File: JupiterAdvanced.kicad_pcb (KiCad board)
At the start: 2 copper layers, 314.8 x 162.9 mm, 223 parts, among them SW1 SW_Push, U1 PRTR5V0U2X, U2 AT90USB1286-AU, Y1 16MHz

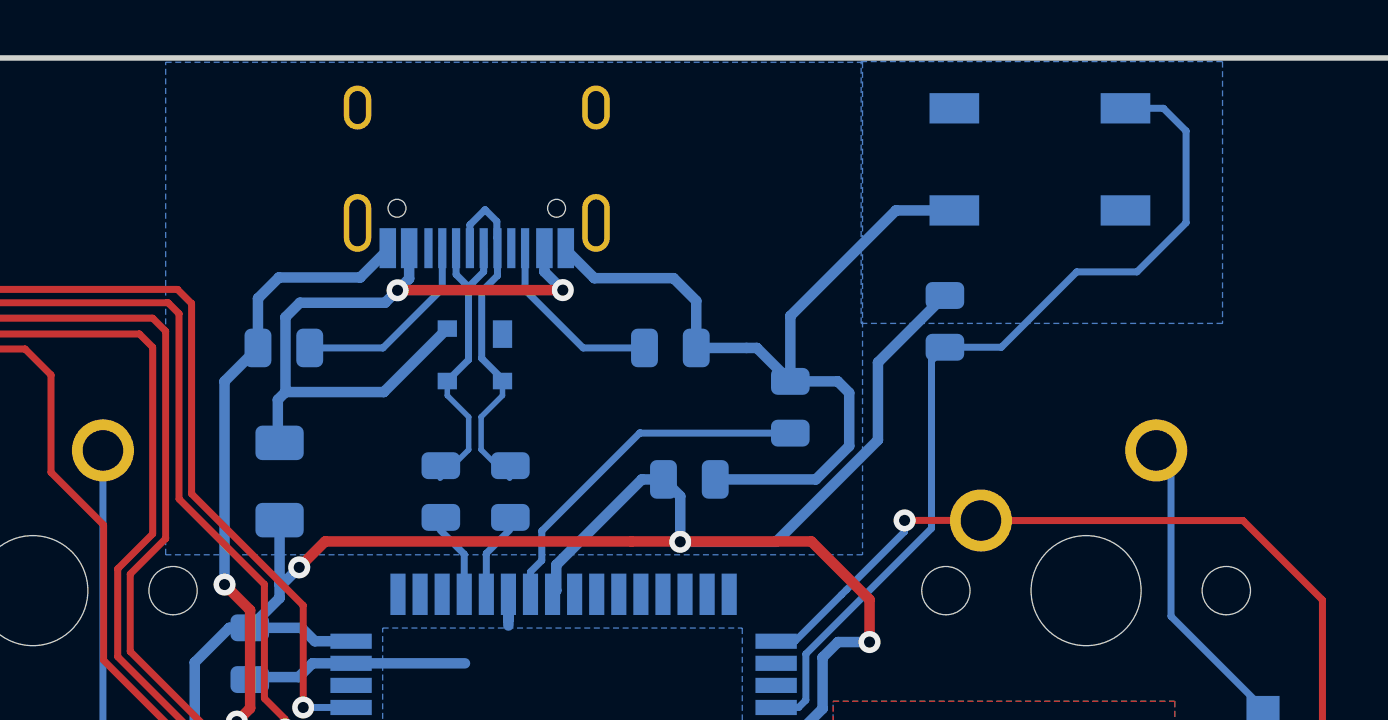
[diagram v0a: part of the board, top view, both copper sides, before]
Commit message: Ferret Bead added on USB Ground
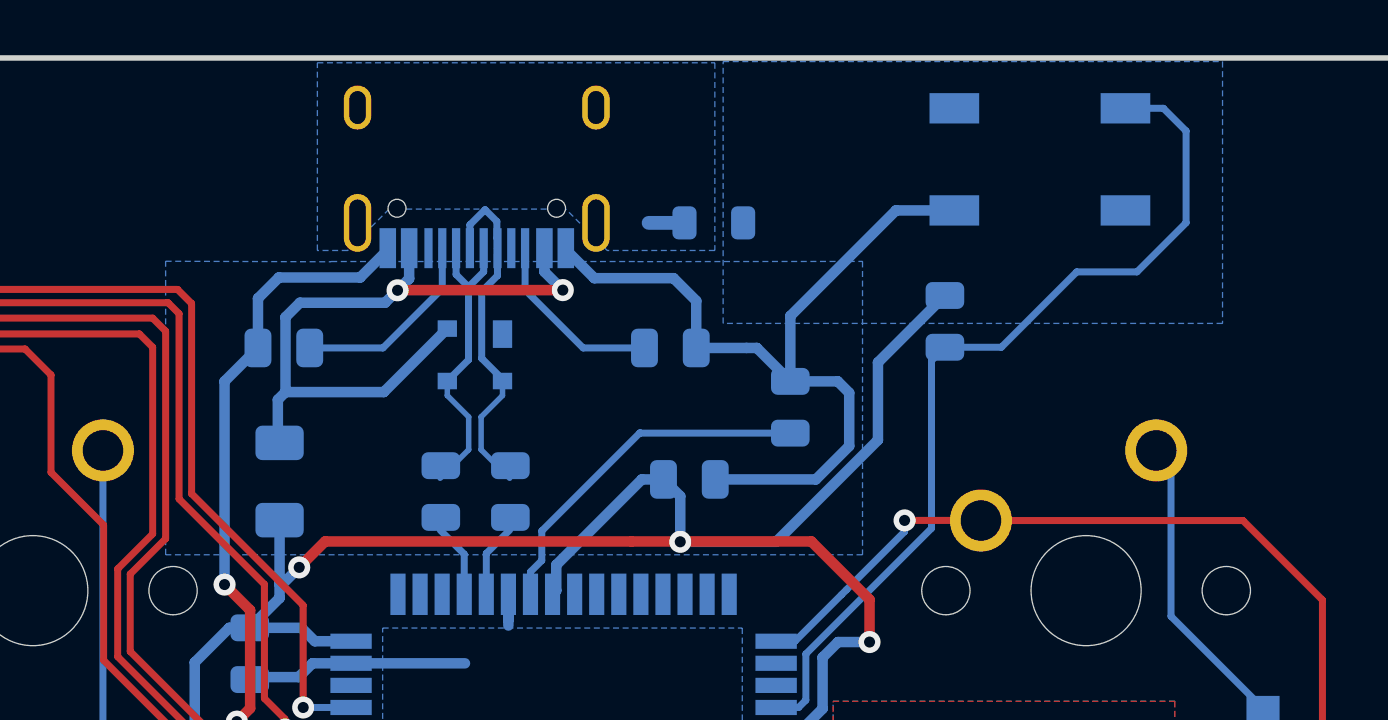
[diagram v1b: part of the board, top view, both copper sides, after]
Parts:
- added FB1: 60@100MHz, Inductor_SMD:L_0805_2012Metric, B.Cu at (271.2, 87.5)
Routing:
- net Earth: track 0.00 -> 1.30 mm

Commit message: Mounting holes updated
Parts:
- H1, H2, H3, H4, H5, H6: footprint MountingHole:MountingHole_2.5mm -> MountingHole:MountingHole_2.5mm_Pad
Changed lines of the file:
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@@
     (add_net VCC)
+  )
+  (module MountingHole:MountingHole_2.5mm_Pad (layer F.Cu)
+    (at 294.02 157.761)
+    (descr "Mounting Hole 2.5mm")
+    (tags "mounting hole 2.5mm")
+    (attr virtual)
+    (fp_text reference H6 (at 0 -3.5) (layer F.SilkS)
+      (effects (font (size 1 1) (thickness 0.15)))
+    )
+    (fp_text value MountingHole (at 0 3.5) (layer F.Fab)
+      (effects (font (size 1 1) (thickness 0.15)))
+    )
+    (fp_text user %R (at 0.3 0) (layer F.Fab)
+      (effects (font (size 1 1) (thickness 0.15)))
+    )
+    (fp_circle (center 0 0) (end 2.5 0) (layer Cmts.User) (width 0.15))
+    (fp_circle (center 0 0) (end 2.75 0) (layer F.CrtYd) (width 0.05))
+    (pad 1 thru_hole circle (at 0 0) (size 5 5) (drill 2.5) (layers *.Cu *.Mask))
+  )
+  (module MountingHole:MountingHole_2.5mm_Pad (layer F.Cu)
+    (at 141.778 157.761)
+    (descr "Mounting Hole 2.5mm")
+    (tags "mounting hole 2.5mm")
+    (attr virtual)
+    (fp_text reference H5 (at 0 -3.5) (layer F.SilkS)
+      (effects (font (size 1 1) (thickness 0.15)))
+    )
+    (fp_text value MountingHole (at 0 3.5) (layer F.Fab)
+      (effects (font (size 1 1) (thickness 0.15)))
+    )
+    (fp_text user %R (at 0.3 0) (layer F.Fab)
+      (effects (font (size 1 1) (thickness 0.15)))
+    )
+    (fp_circle (center 0 0) (end 2.5 0) (layer Cmts.User) (width 0.15))
+    (fp_circle (center 0 0) (end 2.75 0) (layer F.CrtYd) (width 0.05))
+    (pad 1 thru_hole circle (at 0 0) (size 5 5) (drill 2.5) (layers *.Cu *.Mask))
+  )
+  (module MountingHole:MountingHole_2.5mm_Pad (layer F.Cu)
+    (at 65.325 239.475)
+    (descr "Mounting Hole 2.5mm")
+    (tags "mounting hole 2.5mm")
+    (attr virtual)
+    (fp_text reference H4 (at 0 -3.5) (layer F.SilkS)
+      (effects (font (size 1 1) (thickness 0.15)))
+    )
+    (fp_text value MountingHole (at 0 3.5) (layer F.Fab)
+      (effects (font (size 1 1) (thickness 0.15)))
+    )
+    (fp_text user %R (at 0.3 0) (layer F.Fab)
+      (effects (font (size 1 1) (thickness 0.15)))
+    )
+    (fp_circle (center 0 0) (end 2.5 0) (layer Cmts.User) (width 0.15))
+    (fp_circle (center 0 0) (end 2.75 0) (layer F.CrtYd) (width 0.05))
+    (pad 1 thru_hole circle (at 0 0) (size 5 5) (drill 2.5) (layers *.Cu *.Mask))
+  )
+  (module MountingHole:MountingHole_2.5mm_Pad (layer F.Cu)
+    (at 370.325 239.475)
+    (descr "Mounting Hole 2.5mm")
+    (tags "mounting hole 2.5mm")
+    (attr virtual)
+    (fp_text reference H3 (at 0 -3.5) (layer F.SilkS)
+      (effects (font (size 1 1) (thickness 0.15)))
+    )
+    (fp_text value MountingHole (at 0 3.5) (layer F.Fab)
+      (effects (font (size 1 1) (thickness 0.15)))
+    )
+    (fp_text user %R (at 0.3 0) (layer F.Fab)
+      (effects (font (size 1 1) (thickness 0.15)))
+    )
+    (fp_circle (center 0 0) (end 2.5 0) (layer Cmts.User) (width 0.15))
+    (fp_circle (center 0 0) (end 2.75 0) (layer F.CrtYd) (width 0.05))
+    (pad 1 thru_hole circle (at 0 0) (size 5 5) (drill 2.5) (layers *.Cu *.Mask))
+  )
+  (module MountingHole:MountingHole_2.5mm_Pad (layer F.Cu)
+    (at 370.325 86.618)
+    (descr "Mounting Hole 2.5mm")
+    (tags "mounting hole 2.5mm")
+    (attr virtual)
+    (fp_text reference H2 (at 0 -3.5) (layer F.SilkS)
+      (effects (font (size 1 1) (thickness 0.15)))
+    )
+    (fp_text value MountingHole (at 0 3.5) (layer F.Fab)
+      (effects (font (size 1 1) (thickness 0.15)))
+    )
+    (fp_text user %R (at 0.3 0) (layer F.Fab)
+      (effects (font (size 1 1) (thickness 0.15)))
+    )
+    (fp_circle (center 0 0) (end 2.5 0) (layer Cmts.User) (width 0.15))
+    (fp_circle (center 0 0) (end 2.75 0) (layer F.CrtYd) (width 0.05))
+    (pad 1 thru_hole circle (at 0 0) (size 5 5) (drill 2.5) (layers *.Cu *.Mask))
+  )
+  (module MountingHole:MountingHole_2.5mm_Pad (layer F.Cu)
+    (at 65.325 86.518)
+    (descr "Mounting Hole 2.5mm")
+    (tags "mounting hole 2.5mm")
+    (attr virtual)
+    (fp_text reference H1 (at 0 -3.5) (layer F.SilkS)
+      (effects (font (size 1 1) (thickness 0.15)))
+    )
+    (fp_text value MountingHole (at 0 3.5) (layer F.Fab)
+      (effects (font (size 1 1) (thickness 0.15)))
+    )
+    (fp_text user %R (at 0.3 0) (layer F.Fab)
+      (effects (font (size 1 1) (thickness 0.15)))
+    )
+    (fp_circle (center 0 0) (end 2.5 0) (layer Cmts.User) (width 0.15))
+    (fp_circle (center 0 0) (end 2.75 0) (layer F.CrtYd) (width 0.05))
+    (pad 1 thru_hole circle (at 0 0) (size 5 5) (drill 2.5) (layers *.Cu *.Mask))
   )
   (module Inductor_SMD:L_0805_2012Metric (layer B.Cu)
@@
     )
   )
-  (module MountingHole:MountingHole_2.5mm (layer F.Cu)
-    (at 294.02 157.761)
-    (descr "Mounting Hole 2.5mm, no annular")
-    (tags "mounting hole 2.5mm no annular")
-    (attr virtual)
-    (fp_text reference H6 (at 0 -3.5) (layer F.SilkS)
-      (effects (font (size 1 1) (thickness 0.15)))
-    )
-    (fp_text value MountingHole (at 0 3.5) (layer F.Fab)
-      (effects (font (size 1 1) (thickness 0.15)))
-    )
-    (fp_circle (center 0 0) (end 2.5 0) (layer Cmts.User) (width 0.15))
-    (fp_circle (center 0 0) (end 2.75 0) (layer F.CrtYd) (width 0.05))
-    (fp_text user %R (at 0.3 0) (layer F.Fab)
-      (effects (font (size 1 1) (thickness 0.15)))
-    )
-    (pad 1 np_thru_hole circle (at 0 0) (size 2.5 2.5) (drill 2.5) (layers *.Cu *.Mask))
-  )
-  (module MountingHole:MountingHole_2.5mm (layer F.Cu)
-    (at 141.778 157.761)
-    (descr "Mounting Hole 2.5mm, no annular")
-    (tags "mounting hole 2.5mm no annular")
-    (attr virtual)
-    (fp_text reference H5 (at 0 -3.5) (layer F.SilkS)
-      (effects (font (size 1 1) (thickness 0.15)))
-    )
-    (fp_text value MountingHole (at 0 3.5) (layer F.Fab)
-      (effects (font (size 1 1) (thickness 0.15)))
-    )
-    (fp_circle (center 0 0) (end 2.5 0) (layer Cmts.User) (width 0.15))
-    (fp_circle (center 0 0) (end 2.75 0) (layer F.CrtYd) (width 0.05))
-    (fp_text user %R (at 0.3 0) (layer F.Fab)
-      (effects (font (size 1 1) (thickness 0.15)))
-    )
-    (pad 1 np_thru_hole circle (at 0 0) (size 2.5 2.5) (drill 2.5) (layers *.Cu *.Mask))
-  )
-  (module MountingHole:MountingHole_2.5mm (layer F.Cu)
-    (at 65.325 239.475)
-    (descr "Mounting Hole 2.5mm, no annular")
-    (tags "mounting hole 2.5mm no annular")
-    (attr virtual)
-    (fp_text reference H4 (at 0 -3.5) (layer F.SilkS)
-      (effects (font (size 1 1) (thickness 0.15)))
-    )
-    (fp_text value MountingHole (at 0 3.5) (layer F.Fab)
-      (effects (font (size 1 1) (thickness 0.15)))
-    )
-    (fp_circle (center 0 0) (end 2.75 0) (layer F.CrtYd) (width 0.05))
-    (fp_circle (center 0 0) (end 2.5 0) (layer Cmts.User) (width 0.15))
-    (fp_text user %R (at 0.3 0) (layer F.Fab)
-      (effects (font (size 1 1) (thickness 0.15)))
-    )
-    (pad 1 np_thru_hole circle (at 0 0) (size 2.5 2.5) (drill 2.5) (layers *.Cu *.Mask))
-  )
-  (module MountingHole:MountingHole_2.5mm (layer F.Cu)
-    (at 370.325 239.475)
-    (descr "Mounting Hole 2.5mm, no annular")
-    (tags "mounting hole 2.5mm no annular")
-    (attr virtual)
-    (fp_text reference H3 (at 0 -3.5) (layer F.SilkS)
-      (effects (font (size 1 1) (thickness 0.15)))
-    )
-    (fp_text value MountingHole (at 0 3.5) (layer F.Fab)
-      (effects (font (size 1 1) (thickness 0.15)))
-    )
-    (fp_circle (center 0 0) (end 2.75 0) (layer F.CrtYd) (width 0.05))
-    (fp_circle (center 0 0) (end 2.5 0) (layer Cmts.User) (width 0.15))
-    (fp_text user %R (at 0.3 0) (layer F.Fab)
-      (effects (font (size 1 1) (thickness 0.15)))
-    )
-    (pad 1 np_thru_hole circle (at 0 0) (size 2.5 2.5) (drill 2.5) (layers *.Cu *.Mask))
-  )
-  (module MountingHole:MountingHole_2.5mm (layer F.Cu)
-    (at 370.325 86.618)
-    (descr "Mounting Hole 2.5mm, no annular")
-    (tags "mounting hole 2.5mm no annular")
-    (attr virtual)
-    (fp_text reference H2 (at 0 -3.5) (layer F.SilkS)
-      (effects (font (size 1 1) (thickness 0.15)))
-    )
-    (fp_text value MountingHole (at 0 3.5) (layer F.Fab)
-      (effects (font (size 1 1) (thickness 0.15)))
-    )
-    (fp_circle (center 0 0) (end 2.75 0) (layer F.CrtYd) (width 0.05))
-    (fp_circle (center 0 0) (end 2.5 0) (layer Cmts.User) (width 0.15))
-    (fp_text user %R (at 0.3 0) (layer F.Fab)
-      (effects (font (size 1 1) (thickness 0.15)))
-    )
-    (pad 1 np_thru_hole circle (at 0 0) (size 2.5 2.5) (drill 2.5) (layers *.Cu *.Mask))
-  )
-  (module MountingHole:MountingHole_2.5mm (layer F.Cu)
-    (at 65.325 86.518)
-    (descr "Mounting Hole 2.5mm, no annular")
-    (tags "mounting hole 2.5mm no annular")
-    (attr virtual)
-    (fp_text reference H1 (at 0 -3.5) (layer F.SilkS)
-      (effects (font (size 1 1) (thickness 0.15)))
-    )
-    (fp_text value MountingHole (at 0 3.5) (layer F.Fab)
-      (effects (font (size 1 1) (thickness 0.15)))
-    )
-    (fp_circle (center 0 0) (end 2.75 0) (layer F.CrtYd) (width 0.05))
-    (fp_circle (center 0 0) (end 2.5 0) (layer Cmts.User) (width 0.15))
-    (fp_text user %R (at 0.3 0) (layer F.Fab)
-      (effects (font (size 1 1) (thickness 0.15)))
-    )
-    (pad 1 np_thru_hole circle (at 0 0) (size 2.5 2.5) (drill 2.5) (layers *.Cu *.Mask))
-  )
   (module Resistor_SMD:R_0805_2012Metric (layer B.Cu)

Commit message: ATMega32u4 MCU added
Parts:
- removed U2: AT90USB1286-AU, Package_QFP:TQFP-64_14x14mm_P0.8mm
- added U10: ATmega32U4-AU, Package_QFP:TQFP-44_10x10mm_P0.8mm, B.Cu at (265.7, 108.5)
- H1, H2, H3, H4, H5, H6: footprint MountingHole:MountingHole_2.5mm_Pad -> MountingHole:MountingHole_2.5mm
- moved R7 5.09 mm to (260.4, 116.8)
- turned C3 to 90 degrees
- turned C7 to 90 degrees
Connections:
- C7 pad 1: GND -> Net-(C7-Pad1)
- C7 pad 2: Net-(C7-Pad2) -> GND
- R7 pad 1: Net-(R7-Pad1) -> GND
- R7 pad 2: GND -> Net-(R7-Pad2)
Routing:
- net ROW1: track 524.6 -> 497.9 mm
- net ROW2: track 546.7 -> 521.5 mm
- net ROW4: track 584.9 -> 562.3 mm
- net GND: track 119.5 -> 97.0 mm, vias 5 -> 4
- net COL3: track 853.1 -> 831.8 mm
- net ROW5: track 579.1 -> 562.0 mm
- net ROW6: track 620.8 -> 603.7 mm
- net ROW0: track 487.4 -> 470.3 mm
- net Net-(C7-Pad1): track 0.00 -> 15.1 mm
- net COL7: track 188.3 -> 175.3 mm, vias 3 -> 2
- net COL6: track 228.0 -> 215.0 mm, vias 3 -> 2
- net Net-(C7-Pad2): track 12.9 -> 0.00 mm
- net +5V: track 87.0 -> 94.1 mm
- net COL10: track 121.4 -> 128.0 mm
- net COL15: track 243.9 -> 250.2 mm
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
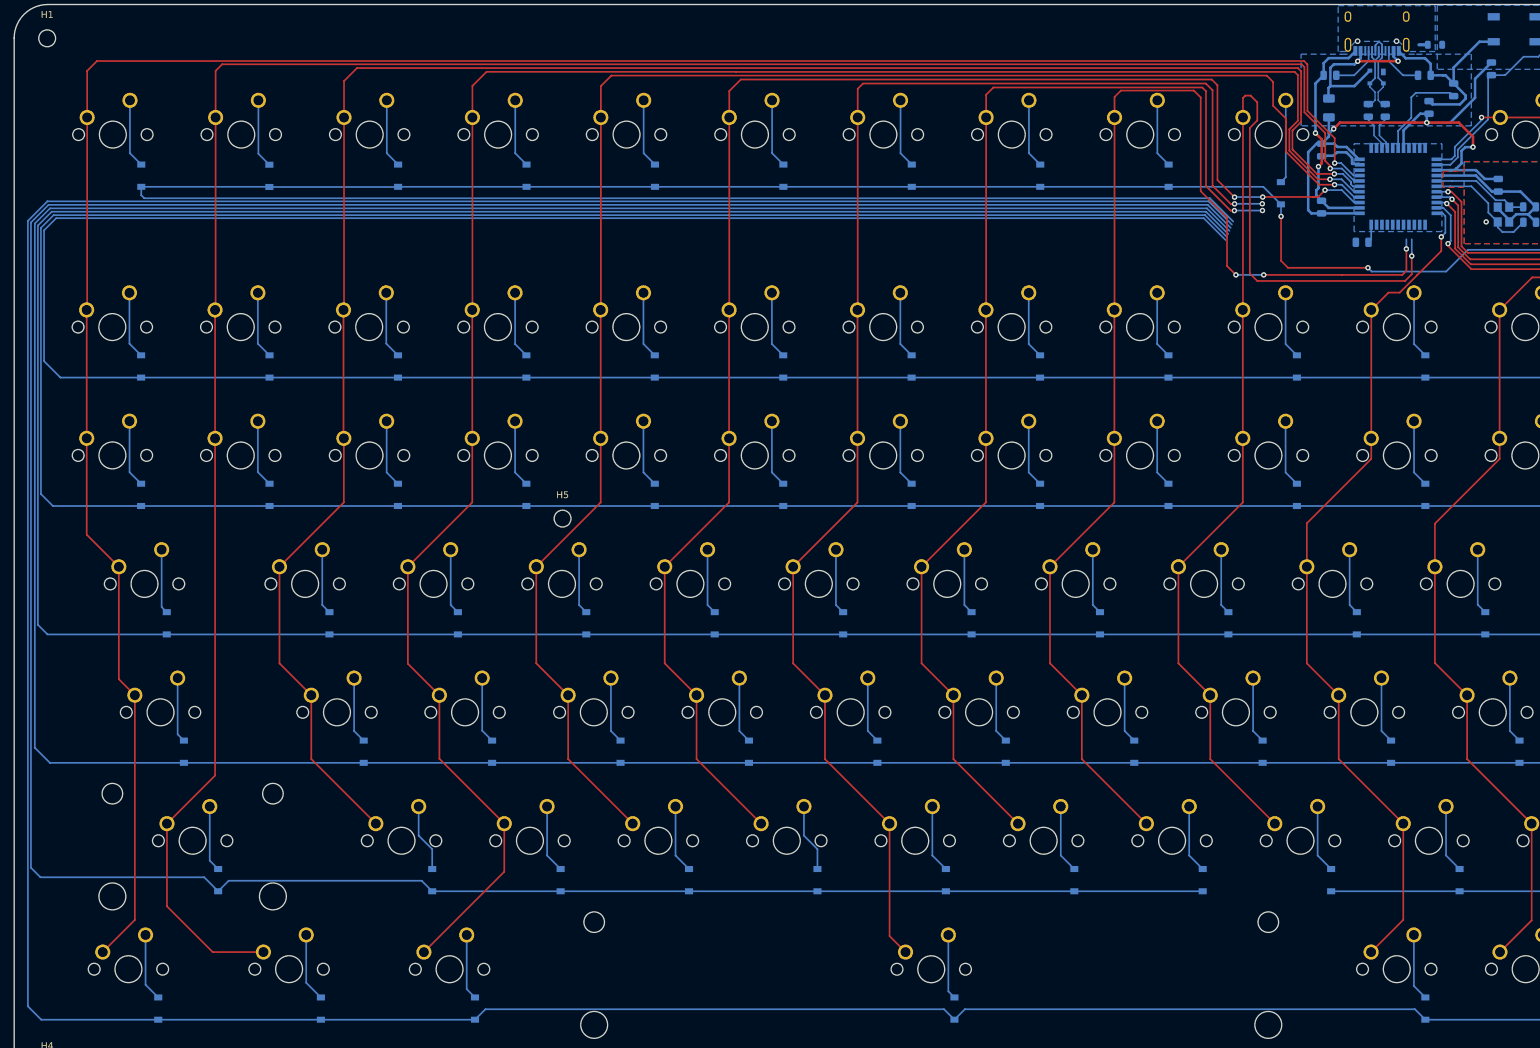
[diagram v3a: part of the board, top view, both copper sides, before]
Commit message: Matrix reconnect, still missing some pins.
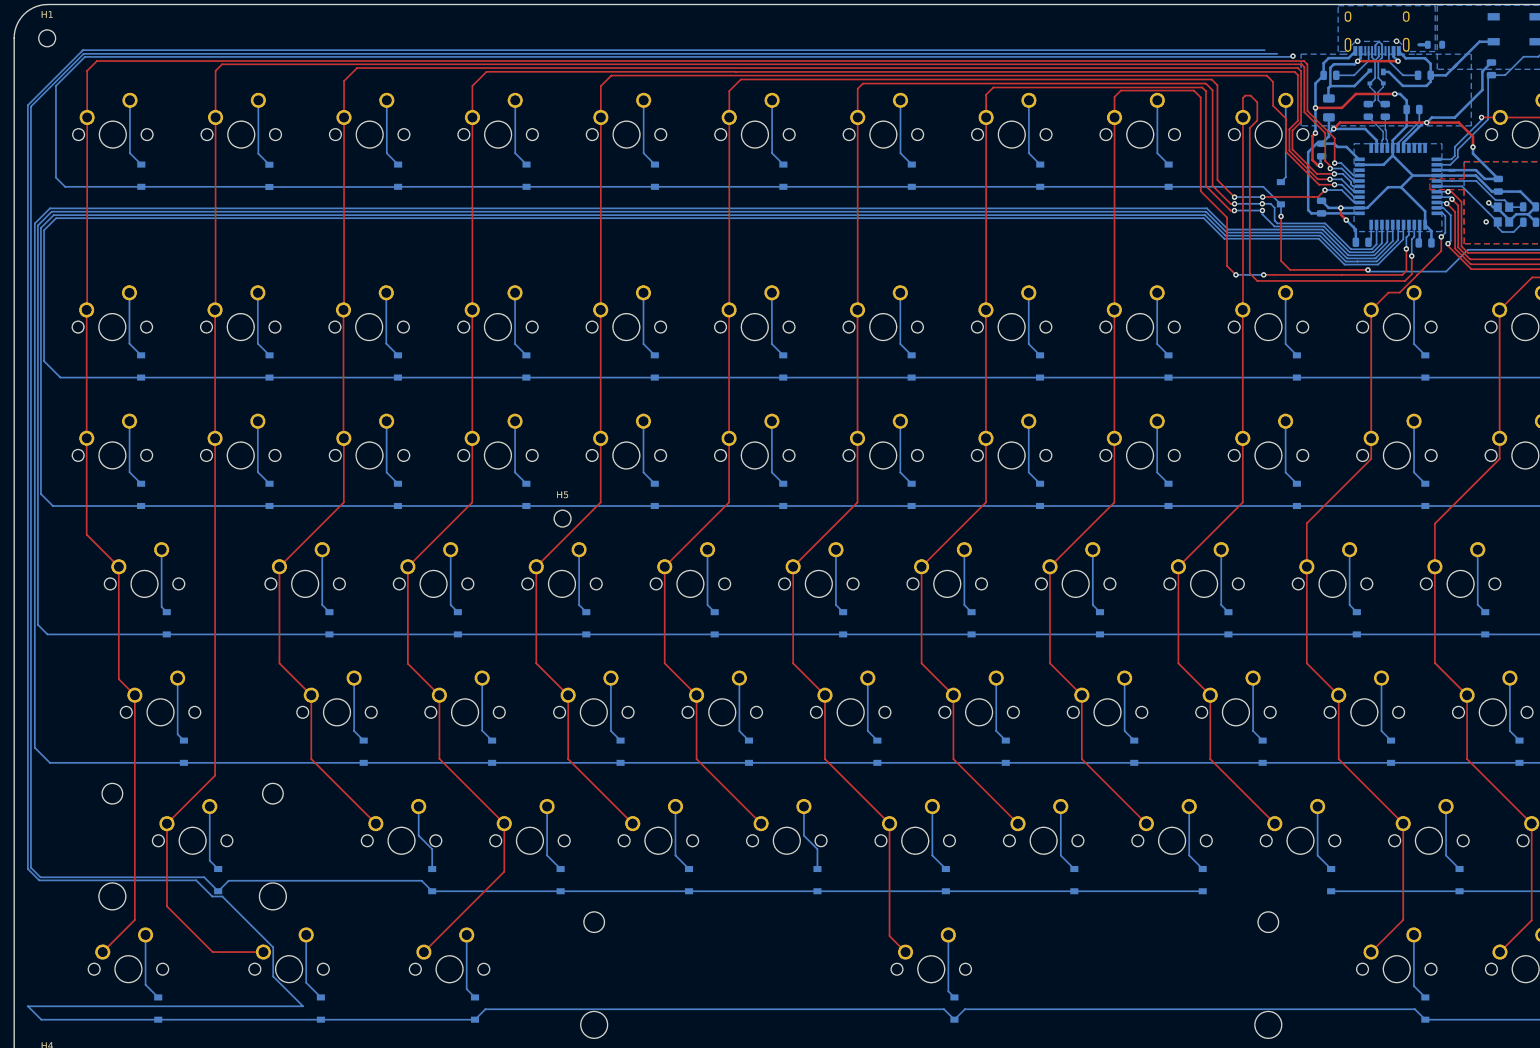
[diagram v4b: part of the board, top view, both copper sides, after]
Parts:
- moved C3 20.1 mm to (269.7, 116.9), turned to 0 degrees
- moved C7 6.70 mm to (267.9, 97.1), turned to 180 degrees
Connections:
- U10 pad 11: ROW4 -> ROW6
- U10 pad 25: Net-(U10-Pad25) -> COL9
- U10 pad 26: Net-(U10-Pad26) -> COL8
- U10 pad 27: Net-(U10-Pad27) -> ROW1
- U10 pad 28: COL3 -> ROW2
- U10 pad 29: ROW2 -> COL3
- U10 pad 30: ROW1 -> ROW4
- U10 pad 31: COL6 -> COL7
- U10 pad 32: COL7 -> COL6
- U10 pad 8: ROW0 -> Net-(U10-Pad8)
- U10 pad 9: ROW6 -> ROW0
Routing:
- net ROW6: track 603.7 -> 698.7 mm
- net GND: track 97.0 -> 149.2 mm, vias 4 -> 9
- net ROW0: track 470.3 -> 517.7 mm, vias 2 -> 3
- net ROW1: track 497.9 -> 529.5 mm
- net ROW2: track 521.5 -> 552.0 mm
- net COL3: track 831.8 -> 861.2 mm
- net ROW4: track 562.3 -> 590.6 mm
- net ROW5: track 562.0 -> 586.8 mm
- net COL6: track 215.0 -> 239.0 mm
- net COL7: track 175.3 -> 199.2 mm
- net +5V: track 94.1 -> 102.8 mm
- net Net-(C7-Pad1): track 15.1 -> 7.00 mm
- net COL9: track 176.1 -> 178.4 mm
- net COL8: track 190.0 -> 192.3 mm
- net DN: track 5.17 -> 6.17 mm
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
